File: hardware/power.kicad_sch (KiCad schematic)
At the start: 100 parts, among them J3 Vcore_sel, U1 TLV62569DBV, U2 TLV62569DBV, U3 MPM3833CGRH-Z, U4 CCGM1A1, U5 TLV62569DBV, U6 TLV62569DBV

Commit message: Adding SDRAM - missing 3 pins
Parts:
- L4: footprint (none) -> Resistor_SMD:R_0402_1005Metric
- U3: footprint apparillo-lib:MPM3833CGRH-Z -> ulx5m-gs:MPM3833CGRH-Z
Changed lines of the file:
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@@
 			)
 		)
-		(property "Footprint" ""
+		(property "Footprint" "Resistor_SMD:R_0402_1005Metric"
 			(at 54.61 175.26 0)
 			(effects
@@
 			)
 		)
-		(property "Footprint" "apparillo-lib:MPM3833CGRH-Z"
+		(property "Footprint" "ulx5m-gs:MPM3833CGRH-Z"
 			(at 63.5 24.384 0)
 			(effects

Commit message: PCB - sorting power supplys
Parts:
- L1: footprint Connector_PinHeader_2.54mm:PinHeader_1x03_P2.54mm_Vertical -> Inductor_SMD:L_1008_2520Metric
- L2, L3, L4: footprint Resistor_SMD:R_0402_1005Metric -> Inductor_SMD:L_1008_2520Metric
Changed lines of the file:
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@@
 			)
 		)
-		(property "Footprint" "Resistor_SMD:R_0402_1005Metric"
+		(property "Footprint" "Inductor_SMD:L_1008_2520Metric"
 			(at 54.61 175.26 0)
 			(effects
@@
 			)
 		)
-		(property "Footprint" "Resistor_SMD:R_0402_1005Metric"
+		(property "Footprint" "Inductor_SMD:L_1008_2520Metric"
 			(at 54.61 109.22 0)
 			(effects
@@
 			)
 		)
-		(property "Footprint" "Connector_PinHeader_2.54mm:PinHeader_1x03_P2.54mm_Vertical"
+		(property "Footprint" "Inductor_SMD:L_1008_2520Metric"
 			(at 54.61 76.2 0)
 			(effects
@@
 			)
 		)
-		(property "Footprint" "Resistor_SMD:R_0402_1005Metric"
+		(property "Footprint" "Inductor_SMD:L_1008_2520Metric"
 			(at 54.61 142.24 0)
 			(effects

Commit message: Placing caps bellow FPGA
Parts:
- J3: footprint Connector_PinHeader_2.54mm:PinHeader_1x03_P2.54mm_Vertical -> Jumper:SolderJumper-3_P1.3mm_Open_RoundedPad1.0x1.5mm
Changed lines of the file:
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@@
 			)
 		)
-		(property "Footprint" "Connector_PinHeader_2.54mm:PinHeader_1x03_P2.54mm_Vertical"
+		(property "Footprint" "Jumper:SolderJumper-3_P1.3mm_Open_RoundedPad1.0x1.5mm"
 			(at 123.19 45.72 0)
 			(effects

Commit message: Adding USB connector and level converter
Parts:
- U4: footprint Package_BGA:BGA-324_15.0x15.0mm_Layout18x18_P0.8mm_Ball0.45mm_Pad0.4mm_NSMD -> ulx5m-gs:BGA-324_15.0x15.0mm_Layout18x18_P0.8mm_Ball0.45mm_Pad0.4mm_NSMD
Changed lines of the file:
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@@
 			)
 		)
-		(property "Footprint" "Package_BGA:BGA-324_15.0x15.0mm_Layout18x18_P0.8mm_Ball0.45mm_Pad0.4mm_NSMD"
+		(property "Footprint" "ulx5m-gs:BGA-324_15.0x15.0mm_Layout18x18_P0.8mm_Ball0.45mm_Pad0.4mm_NSMD"
 			(at 228.6 96.52 0)
 			(effects

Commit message: Routing diff clock
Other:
- company: (none) -> ${project_creator}
- title: (none) -> ${project_name}
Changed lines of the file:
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@@
 	(generator_version "9.0")
 	(paper "A4")
+	(title_block
+		(title "${project_name}")
+		(date "2025-06-24")
+		(rev "${project_version}")
+		(company "${project_creator}")
+		(comment 1 "${project_license}")
+	)
 	(rectangle
 		(start 238.76 120.65)

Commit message: Routing
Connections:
- net VDD_CORE: no longer TP10.1, TP6.1, TP8.1
- net VDD_PLL: now also TP6.1
- net VDD_SER: now also TP10.1
- net VDD_SER_PLL: now also TP8.1
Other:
- moved on the sheet: TP10, TP6, TP8
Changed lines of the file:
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@@
 	(wire
 		(pts
+			(xy 166.37 72.39) (xy 166.37 76.2)
+		)
+		(stroke
+			(width 0)
+			(type default)
+		)
+	)
+	(wire
+		(pts
 			(xy 106.68 43.18) (xy 116.84 43.18)
 		)
@@
 	(wire
 		(pts
+			(xy 166.37 138.43) (xy 166.37 142.24)
+		)
+		(stroke
+			(width 0)
+			(type default)
+		)
+	)
+	(wire
+		(pts
 			(xy 58.42 83.82) (xy 68.58 83.82)
 		)
@@
 	(wire
 		(pts
+			(xy 166.37 105.41) (xy 166.37 109.22)
+		)
+		(stroke
+			(width 0)
+			(type default)
+		)
+	)
+	(wire
+		(pts
 			(xy 99.06 175.26) (xy 100.33 175.26)
 		)
@@
 	(symbol
 		(lib_id "Connector:TestPoint")
-		(at 148.59 76.2 0)
+		(at 166.37 72.39 0)
 		(unit 1)
 		(exclude_from_sim no)
@@
 		(dnp no)
 		(property "Reference" "TP8"
-			(at 148.59 68.58 0)
+			(at 166.37 64.77 0)
 			(effects
 				(font
@@
 		)
 		(property "Value" "VDD_SER_PLL"
-			(at 142.24 71.12 0)
+			(at 160.02 67.31 0)
 			(effects
 				(font
@@
 		)
 		(property "Footprint" "TestPoint:TestPoint_Pad_D1.0mm"
-			(at 153.67 76.2 0)
+			(at 171.45 72.39 0)
 			(effects
 				(font
@@
 		)
 		(property "Datasheet" "~"
-			(at 153.67 76.2 0)
+			(at 171.45 72.39 0)
 			(effects
 				(font
@@
 		)
 		(property "Description" ""
-			(at 148.59 76.2 0)
+			(at 166.37 72.39 0)
 			(effects
 				(font
@@
 	(symbol
 		(lib_id "Connector:TestPoint")
-		(at 148.59 109.22 0)
+		(at 166.37 105.41 0)
 		(unit 1)
 		(exclude_from_sim no)
@@
 		(dnp no)
 		(property "Reference" "TP10"
-			(at 148.59 101.6 0)
+			(at 166.37 97.79 0)
 			(effects
 				(font
@@
 		)
 		(property "Value" "VDD_SER"
-			(at 144.78 104.14 0)
+			(at 162.56 100.33 0)
 			(effects
 				(font
@@
 		)
 		(property "Footprint" "TestPoint:TestPoint_Pad_D1.0mm"
-			(at 153.67 109.22 0)
+			(at 171.45 105.41 0)
 			(effects
 				(font
@@
 		)
 		(property "Datasheet" "~"
-			(at 153.67 109.22 0)
+			(at 171.45 105.41 0)
 			(effects
 				(font
@@
 		)
 		(property "Description" ""
-			(at 148.59 109.22 0)
+			(at 166.37 105.41 0)
 			(effects
 				(font
@@
 	(symbol
 		(lib_id "Connector:TestPoint")
-		(at 148.59 142.24 0)
+		(at 166.37 138.43 0)
 		(unit 1)
 		(exclude_from_sim no)
@@
 		(dnp no)
 		(property "Reference" "TP6"
-			(at 148.59 134.62 0)
+			(at 166.37 130.81 0)
 			(effects
 				(font
@@
 		)
 		(property "Value" "VDD_PLL"
-			(at 144.78 137.16 0)
+			(at 162.56 133.35 0)
 			(effects
 				(font
@@
 		)
 		(property "Footprint" "TestPoint:TestPoint_Pad_D1.0mm"
-			(at 153.67 142.24 0)
+			(at 171.45 138.43 0)
 			(effects
 				(font
@@
 		)
 		(property "Datasheet" "~"
-			(at 153.67 142.24 0)
+			(at 171.45 138.43 0)
 			(effects
 				(font
@@
 		)
 		(property "Description" ""
-			(at 148.59 142.24 0)
+			(at 166.37 138.43 0)
 			(effects
 				(font

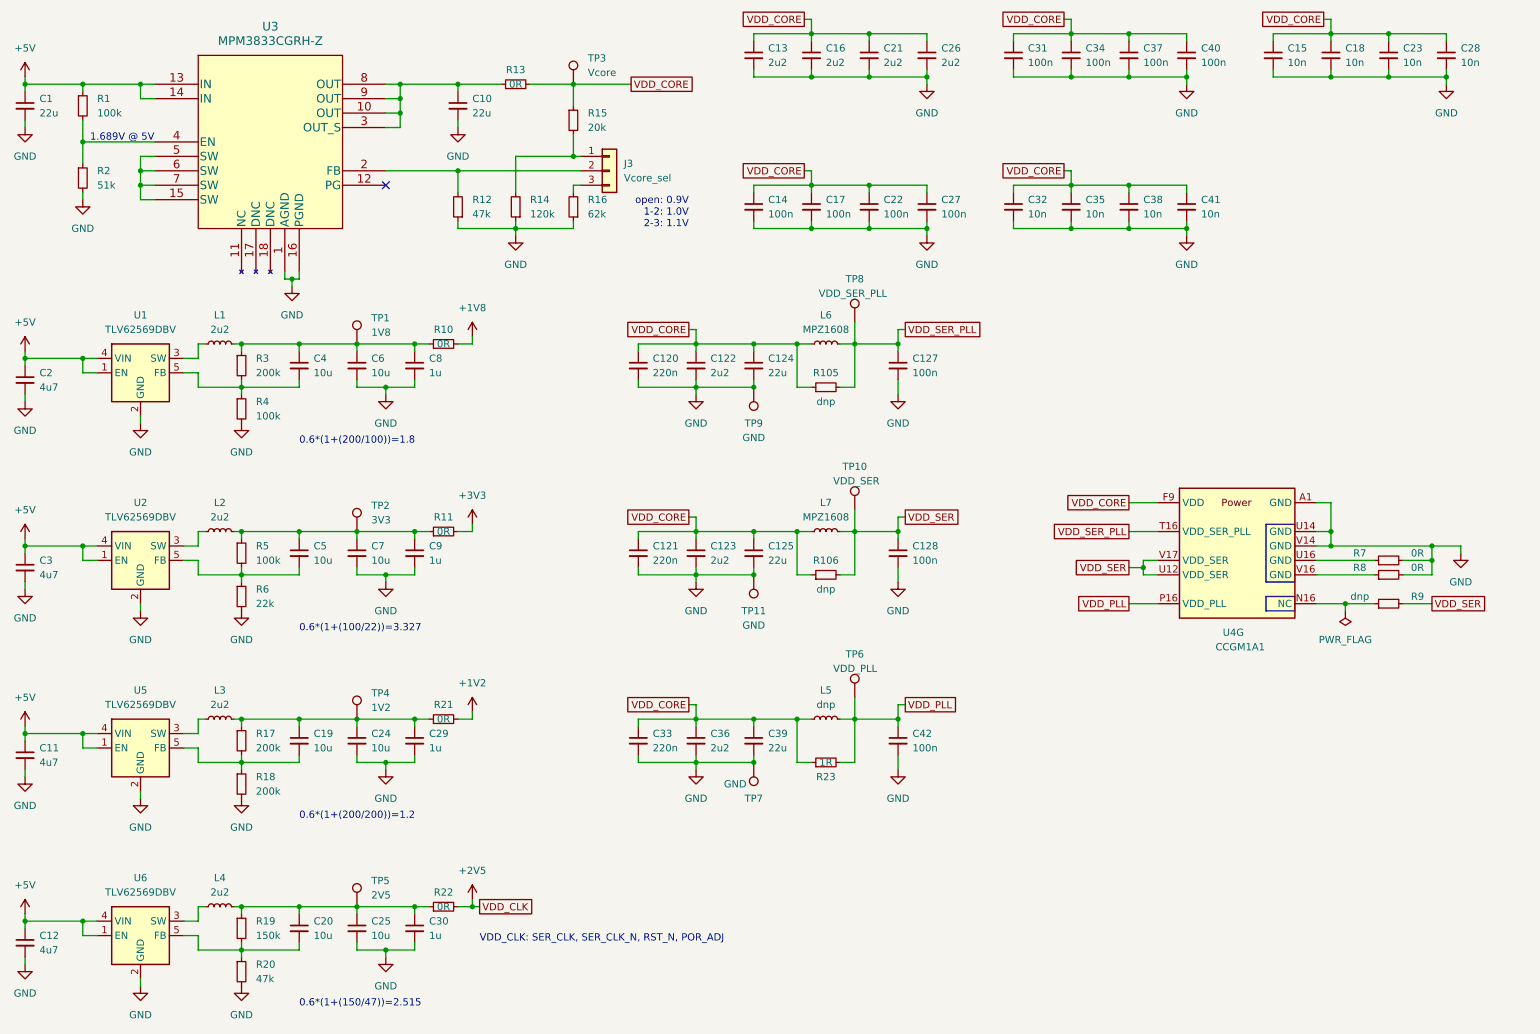
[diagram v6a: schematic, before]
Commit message: Clearing ERC errors/warnings
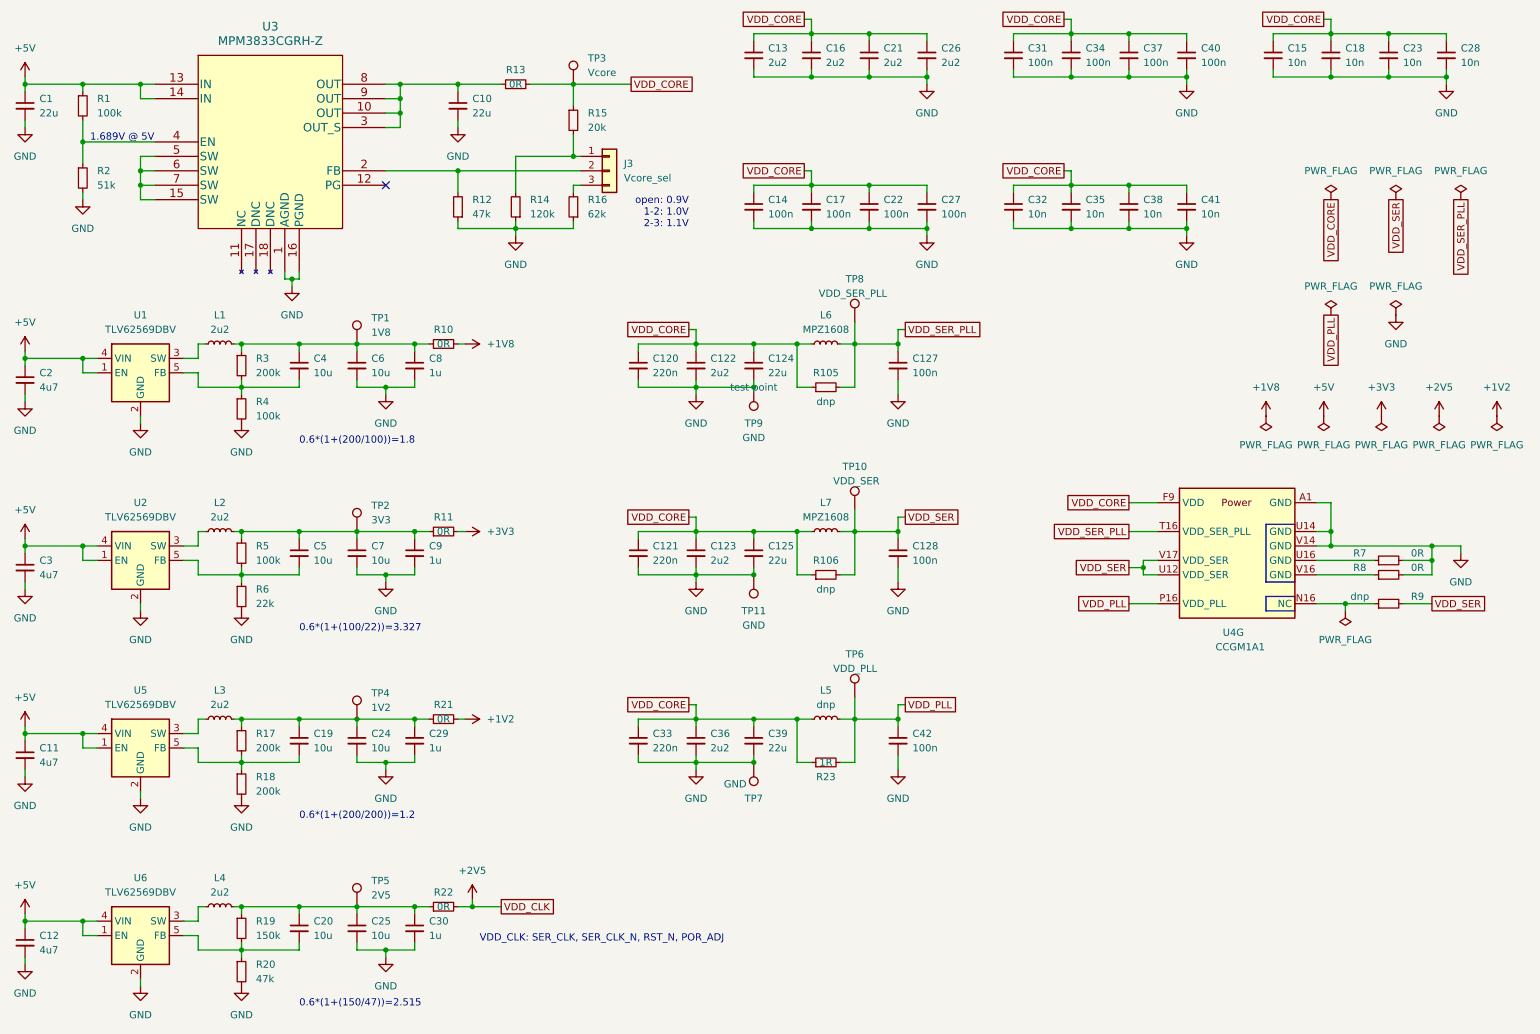
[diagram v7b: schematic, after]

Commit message: Clearing all ERC, rounting diff
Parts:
- U3: footprint ulx5m-gs:MPM3833CGRH-Z -> (none)
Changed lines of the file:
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@@
 			)
 		)
-		(property "Footprint" "ulx5m-gs:MPM3833CGRH-Z"
+		(property "Footprint" ""
 			(at 63.5 24.384 0)
 			(effects
